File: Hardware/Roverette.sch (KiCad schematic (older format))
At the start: 4 parts, among them M1 Motor_DC, M2 Motor_DC

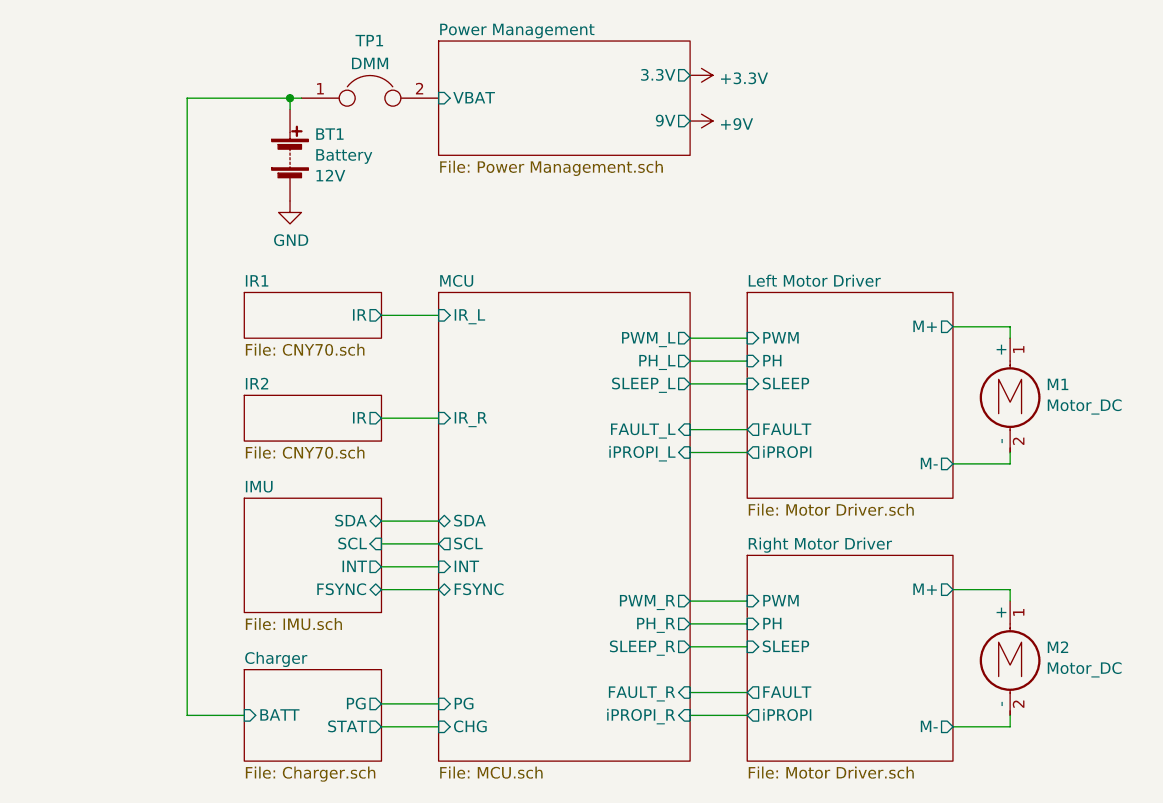
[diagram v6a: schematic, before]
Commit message: Net names declared in root sheet
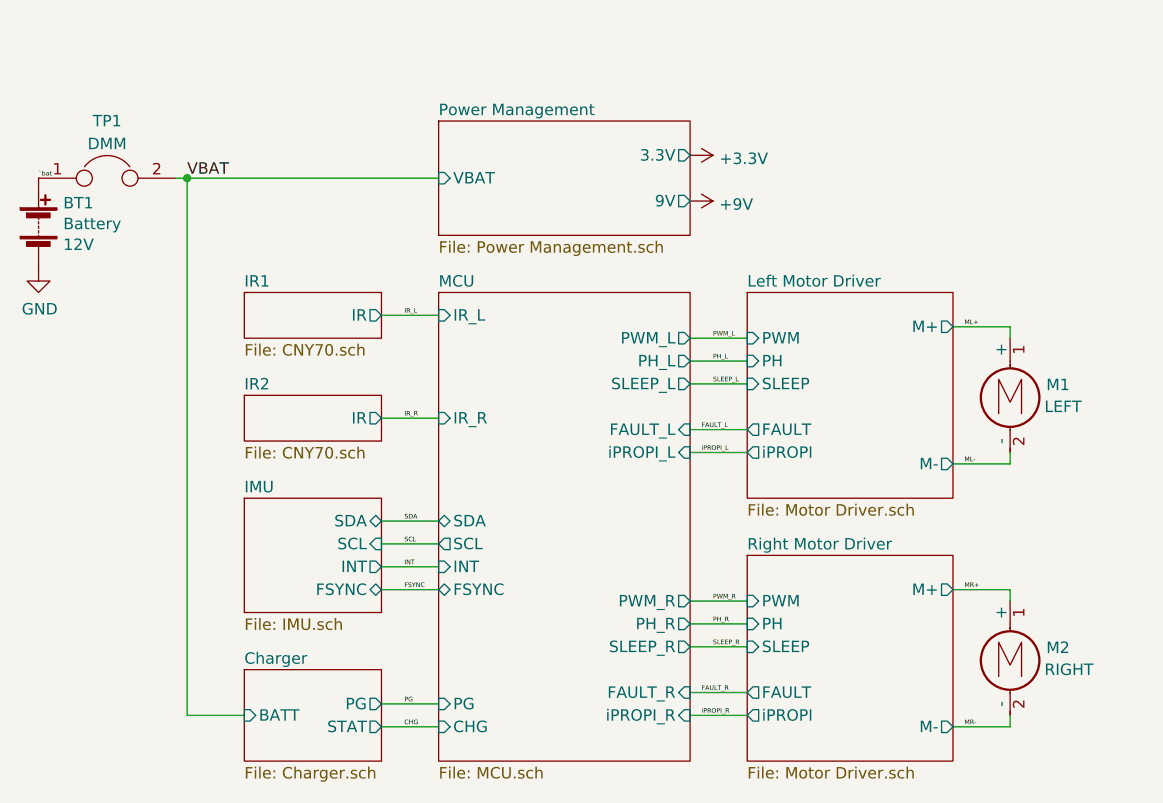
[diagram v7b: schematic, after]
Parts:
- M1: Field4 (none) -> LEFT
- M2: Field4 (none) -> RIGHT
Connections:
- net Charger/BATT renamed `bat
- net Left Motor Driver/M+ renamed ML+
- net Left Motor Driver/M- renamed ML-
- net Power Management/VBAT renamed VBAT
- net Right Motor Driver/M+ renamed MR+
- net Right Motor Driver/M- renamed MR-
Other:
- moved on the sheet: BT1, TP1
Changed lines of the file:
@@
 Sheet 1 9
 Title "Roverette"
-Date "2020-10-11"
+Date "2021-01-01"
 Rev "1.0"
-Comp "Air University Islamabad"
+Comp "RISETech NUST CEME"
 Comment1 "Usman Mehmood"
 Comment2 ""
@@
 P 7500 3550
 F 0 "M1" H 7658 3546 50  0000 L CNN
-F 1 "Motor_DC" H 7658 3455 50  0000 L CNN
+F 1 "Motor_DC" H 7658 3455 50  0001 L CNN
 F 2 "" H 7500 3460 50  0001 C CNN
 F 3 "~" H 7500 3460 50  0001 C CNN
+F 4 "LEFT" H 7650 3450 50  0000 L CNN "Field4"
 	1    7500 3550
 	1    0    0    -1
@@
 P 7500 4700
 F 0 "M2" H 7658 4696 50  0000 L CNN
-F 1 "Motor_DC" H 7658 4605 50  0000 L CNN
+F 1 "Motor_DC" H 7658 4605 50  0001 L CNN
 F 2 "" H 7500 4610 50  0001 C CNN
 F 3 "~" H 7500 4610 50  0001 C CNN
+F 4 "RIGHT" H 7650 4600 50  0000 L CNN "Field4"
 	1    7500 4700
 	1    0    0    -1
@@
 F19 "PWM_L" O R 6100 3350 50
 $EndSheet
-$Comp
-L power:+9V #PWR02
-U 1 1 5FF30D7D
-P 6100 2400
-F 0 "#PWR02" H 6100 2250 50  0001 C CNN
-F 1 "+9V" V 6115 2528 50  0000 L CNN
-F 2 "" H 6100 2400 50  0001 C CNN
-F 3 "" H 6100 2400 50  0001 C CNN
-	1    6100 2400
-	0    1    1    0
-$EndComp
-$Comp
-L power:+3.3V #PWR01
-U 1 1 5FF308D0
-P 6100 2200
-F 0 "#PWR01" H 6100 2050 50  0001 C CNN
-F 1 "+3.3V" V 6115 2328 50  0000 L CNN
-F 2 "" H 6100 2200 50  0001 C CNN
-F 3 "" H 6100 2200 50  0001 C CNN
-	1    6100 2200
-	0    1    1    0
-$EndComp
-Wire Wire Line
-	4350 2300 4350 2350
-$Comp
-L Device:Jumper TP1
-U 1 1 5FF3E3D0
-P 4700 2300
-AR Path="/5FF3E3D0" Ref="TP1"  Part="1"
-AR Path="/5FF0069C/5FF3E3D0" Ref="TP?"  Part="1"
-F 0 "TP1" H 4700 2550 50  0000 C CNN
-F 1 "TestPoint_2Pole" H 4700 2404 50  0001 C CNN
-F 2 "TestPoint:TestPoint_2Pads_Pitch2.54mm_Drill0.8mm" H 4700 2300 50  0001 C CNN
-F 3 "~" H 4700 2300 50  0001 C CNN
-F 4 "DMM" H 4700 2450 50  0000 C CNN "Field4"
-	1    4700 2300
-	1    0    0    -1
-$EndComp
-$Comp
-L power:GND #PWR03
-U 1 1 5FF31DAB
-P 4350 2750
-F 0 "#PWR03" H 4350 2500 50  0001 C CNN
-F 1 "GND" H 4355 2577 50  0000 C CNN
-F 2 "" H 4350 2750 50  0001 C CNN
-F 3 "" H 4350 2750 50  0001 C CNN
-	1    4350 2750
-	1    0    0    -1
-$EndComp
-$Comp
-L Device:Battery BT1
-U 1 1 5FF30336
-P 4350 2550
-F 0 "BT1" H 4458 2641 50  0000 L CNN
-F 1 "Battery" H 4458 2550 50  0000 L CNN
-F 2 "" V 4350 2610 50  0001 C CNN
-F 3 "~" V 4350 2610 50  0001 C CNN
-F 4 "12V" H 4458 2459 50  0000 L CNN "Field4"
-	1    4350 2550
-	1    0    0    -1
-$EndComp
 $Sheet
 S 4150 4050 600  500
@@
 $EndSheet
 Wire Wire Line
-	3900 2300 3900 5000
-Wire Wire Line
 	3900 5000 4150 5000
 Wire Wire Line
@@
 Wire Wire Line
 	6350 3350 6100 3350
-$Sheet
-S 5000 2050 1100 500
+$Comp
+L Device:Battery BT1
+U 1 1 5FF30336
+P 3250 2850
+F 0 "BT1" H 3358 2941 50  0000 L CNN
+F 1 "Battery" H 3358 2850 50  0000 L CNN
+F 2 "" V 3250 2910 50  0001 C CNN
+F 3 "~" V 3250 2910 50  0001 C CNN
+F 4 "12V" H 3358 2759 50  0000 L CNN "Field4"
+	1    3250 2850
+	1    0    0    -1
+$EndComp
+$Comp
+L power:GND #PWR03
+U 1 1 5FF31DAB
+P 3250 3050
+F 0 "#PWR03" H 3250 2800 50  0001 C CNN
+F 1 "GND" H 3255 2877 50  0000 C CNN
+F 2 "" H 3250 3050 50  0001 C CNN
+F 3 "" H 3250 3050 50  0001 C CNN
+	1    3250 3050
+	1    0    0    -1
+$EndComp
+$Sheet
+S 5000 2400 1100 500
 U 5FF0069C
 F0 "Power Management" 50
 F1 "Power Management.sch" 50
-F2 "VBAT" I L 5000 2300 50
-F3 "3.3V" O R 6100 2200 50
-F4 "9V" O R 6100 2400 50
-$EndSheet
-Wire Wire Line
-	4350 2300 3900 2300
-Wire Wire Line
-	4400 2300 4350 2300
-Connection ~ 4350 2300
+F2 "VBAT" I L 5000 2650 50
+F3 "3.3V" O R 6100 2550 50
+F4 "9V" O R 6100 2750 50
+$EndSheet
+$Comp
+L power:+3.3V #PWR01
+U 1 1 5FF308D0
+P 6100 2550
+F 0 "#PWR01" H 6100 2400 50  0001 C CNN
+F 1 "+3.3V" V 6115 2678 50  0000 L CNN
+F 2 "" H 6100 2550 50  0001 C CNN
+F 3 "" H 6100 2550 50  0001 C CNN
+	1    6100 2550
+	0    1    1    0
+$EndComp
+$Comp
+L power:+9V #PWR02
+U 1 1 5FF30D7D
+P 6100 2750
+F 0 "#PWR02" H 6100 2600 50  0001 C CNN
+F 1 "+9V" V 6115 2878 50  0000 L CNN
+F 2 "" H 6100 2750 50  0001 C CNN
+F 3 "" H 6100 2750 50  0001 C CNN
+	1    6100 2750
+	0    1    1    0
+$EndComp
+$Comp
+L Device:Jumper TP1
+U 1 1 5FF3E3D0
+P 3550 2650
+AR Path="/5FF3E3D0" Ref="TP1"  Part="1"
+AR Path="/5FF0069C/5FF3E3D0" Ref="TP?"  Part="1"
+F 0 "TP1" H 3550 2900 50  0000 C CNN
+F 1 "TestPoint_2Pole" H 3550 2754 50  0001 C CNN
+F 2 "TestPoint:TestPoint_2Pads_Pitch2.54mm_Drill0.8mm" H 3550 2650 50  0001 C CNN
+F 3 "~" H 3550 2650 50  0001 C CNN
+F 4 "DMM" H 3550 2800 50  0000 C CNN "Field4"
+	1    3550 2650
+	1    0    0    -1
+$EndComp
+Wire Wire Line
+	5000 2650 3900 2650
+Wire Wire Line
+	3900 2650 3850 2650
+Text Label 3900 2650 0    50   ~ 0
+VBAT
+Text Label 3250 2650 0    20   ~ 0
+`bat
+Connection ~ 3900 2650
+Wire Wire Line
+	3900 2650 3900 5000
+Text Label 6150 5000 0    20   ~ 0
+iPROPI_R
+Text Label 6150 3850 0    20   ~ 0
+iPROPI_L
+Text Label 4850 3700 0    20   ~ 0
+IR_R
+Text Label 6200 3350 0    20   ~ 0
+PWM_L
+Text Label 6200 3450 0    20   ~ 0
+PH_L
+Text Label 6200 3550 0    20   ~ 0
+SLEEP_L
+Text Label 6150 3750 0    20   ~ 0
+FAULT_L
+Text Label 6150 4900 0    20   ~ 0
+FAULT_R
+Text Label 6200 4500 0    20   ~ 0
+PWM_R
+Text Label 6200 4600 0    20   ~ 0
+PH_R
+Text Label 6200 4700 0    20   ~ 0
+SLEEP_R
+Text Label 4850 4950 0    20   ~ 0
+PG
+Text Label 4850 4150 0    20   ~ 0
+SDA
+Text Label 4850 4250 0    20   ~ 0
+SCL
+Text Label 4850 5050 0    20   ~ 0
+CHG
+Text Label 4850 4350 0    20   ~ 0
+INT
+Text Label 4850 4450 0    20   ~ 0
+FSYNC
+Text Label 4850 3250 0    20   ~ 0
+IR_L
+Text Label 7300 3300 0    20   ~ 0
+ML+
+Text Label 7300 3900 0    20   ~ 0
+ML-
+Text Label 7300 4450 0    20   ~ 0
+MR+
+Text Label 7300 5050 0    20   ~ 0
+MR-
 $EndSCHEMATC

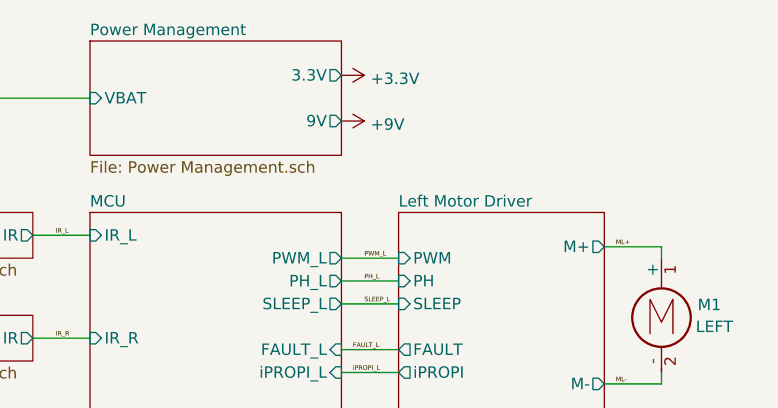
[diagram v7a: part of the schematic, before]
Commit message: Replaced ESP-WROOM-32D with ESP32-CAM
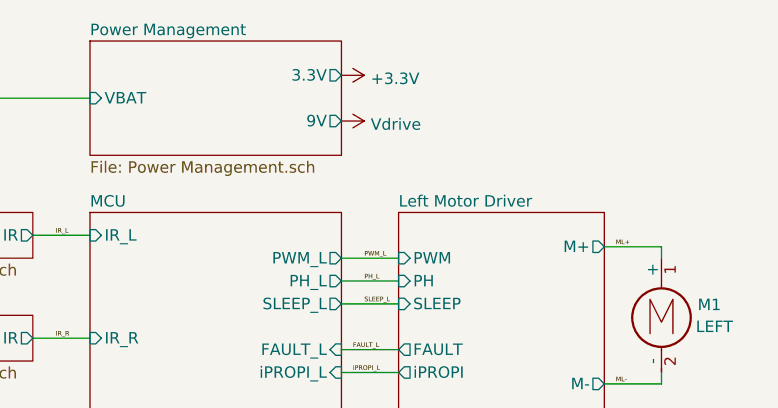
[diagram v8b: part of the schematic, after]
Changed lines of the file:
@@
-$EndComp
-$Comp
-L power:+9V #PWR02
-U 1 1 5FF30D7D
-P 6100 2750
-F 0 "#PWR02" H 6100 2600 50  0001 C CNN
-F 1 "+9V" V 6115 2878 50  0000 L CNN
-F 2 "" H 6100 2750 50  0001 C CNN
-F 3 "" H 6100 2750 50  0001 C CNN
-	1    6100 2750
-	0    1    1    0
 $EndComp
 $Comp
@@
 Text Label 7300 5050 0    20   ~ 0
 MR-
+$Comp
+L power:Vdrive #PWR0101
+U 1 1 5FF4E8AF
+P 6100 2750
+F 0 "#PWR0101" H 5900 2600 50  0001 C CNN
+F 1 "Vdrive" V 6115 2878 50  0000 L CNN
+F 2 "" H 6100 2750 50  0001 C CNN
+F 3 "" H 6100 2750 50  0001 C CNN
+	1    6100 2750
+	0    1    1    0
+$EndComp
 $EndSCHEMATC
